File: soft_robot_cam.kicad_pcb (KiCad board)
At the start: 2 copper layers, 47.5 x 41 mm, 63 parts, among them J1 Conn_01x24_Socket, J2 Screw_Terminal_01x02, J3 Screw_Terminal_01x02, J4 Conn_01x05_Pin, J5 Screw_Terminal_01x02, Q1 S8050, Q2 S8050, SW1 reset, SW2 SW_DPST_x2, U1 DRV8872DDA, U2 DRV8872DDA, U3 ICM-20602, U4 AP2112K-1.2, U5 3.3v, U6 ESP32-WROVER-E, U7 TC2014-2.8VxCTTR

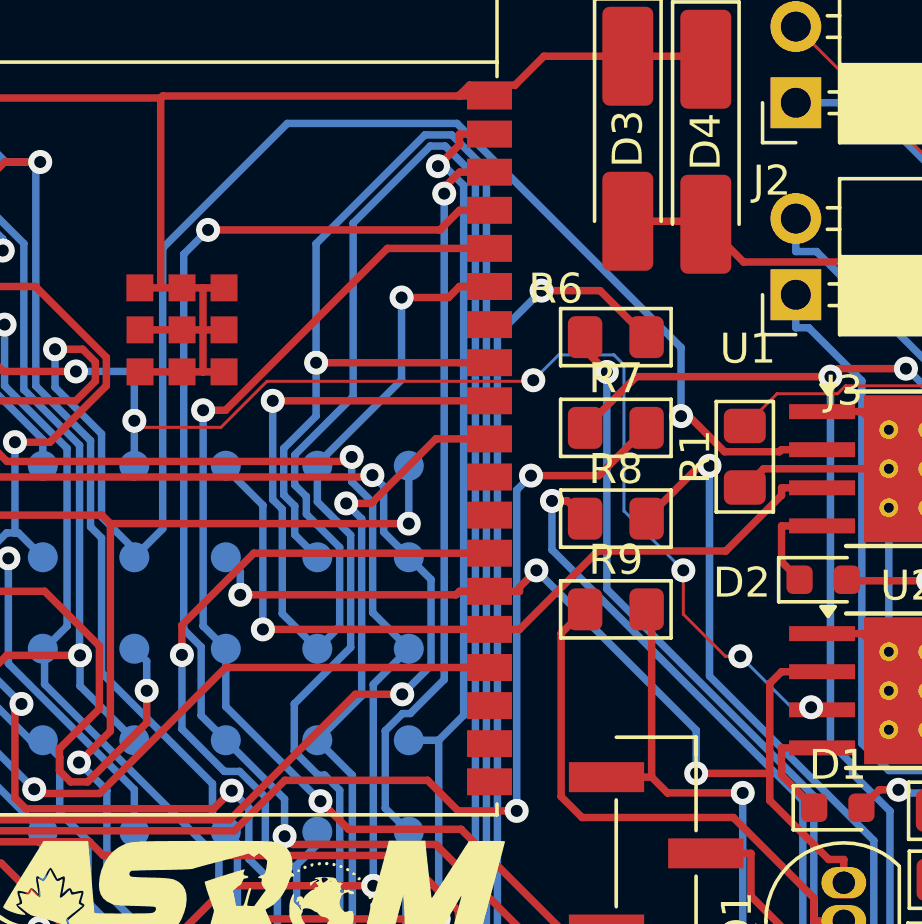
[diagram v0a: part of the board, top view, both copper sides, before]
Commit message: Major overhaul to layout, changed ESP to support more GPIOs, changed IMU to be standardized, changed LDOs to support the correct amperage, added buck converter for shifting LiPo voltage to 3.3V.
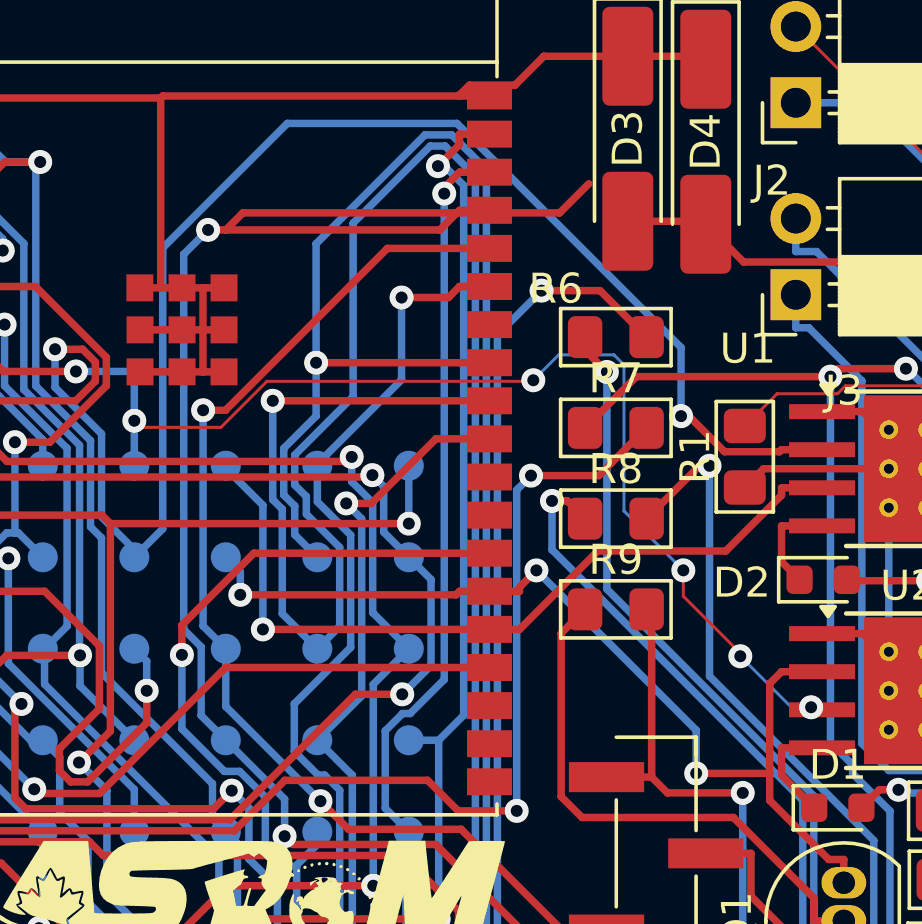
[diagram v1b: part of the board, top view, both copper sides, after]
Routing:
- net TXD_esp: track 48.0 -> 60.7 mm

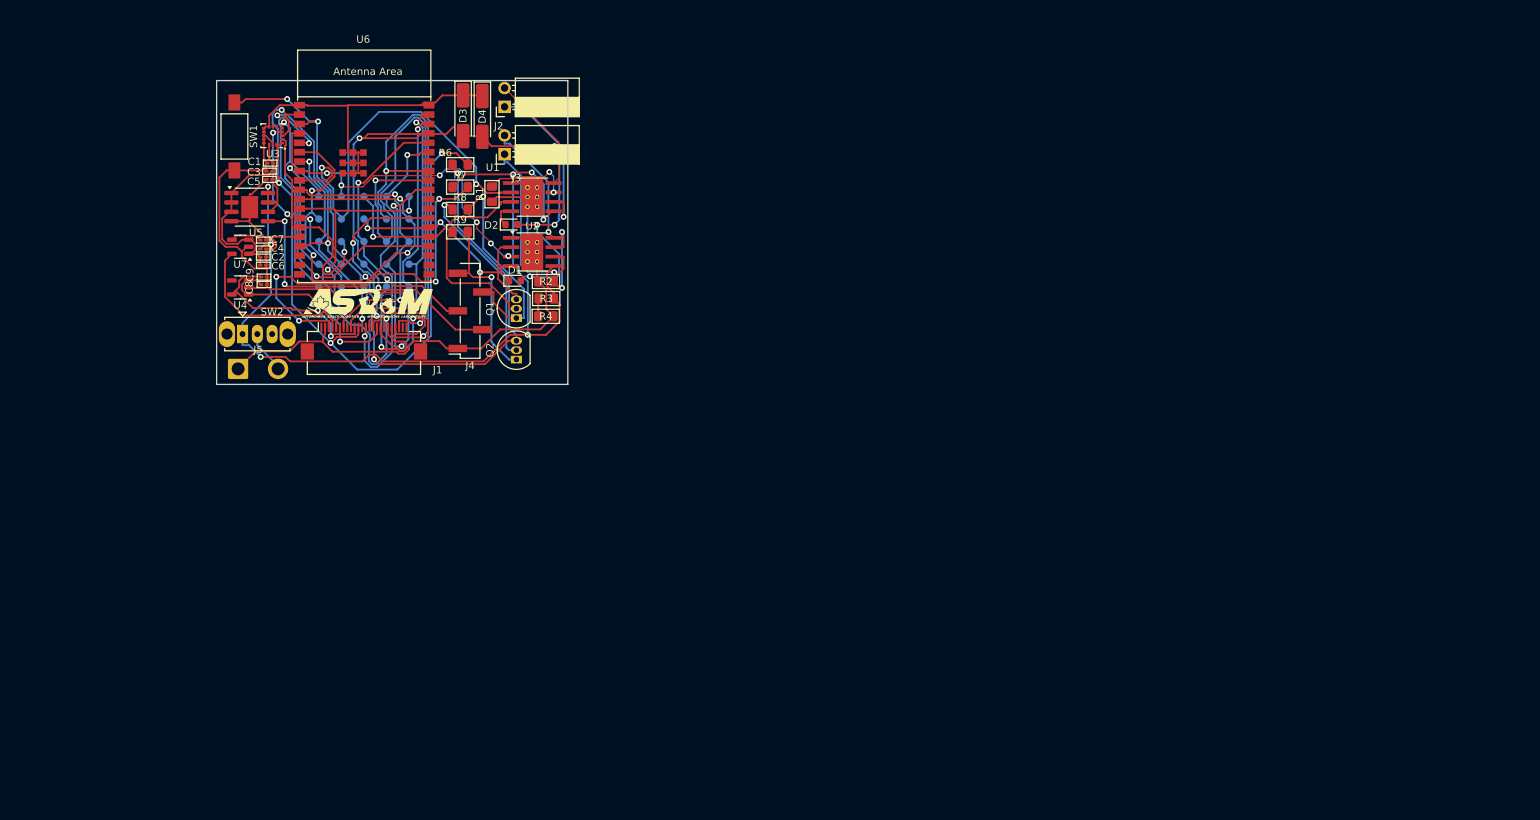
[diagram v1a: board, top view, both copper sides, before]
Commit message: Completed the schematic, began layout
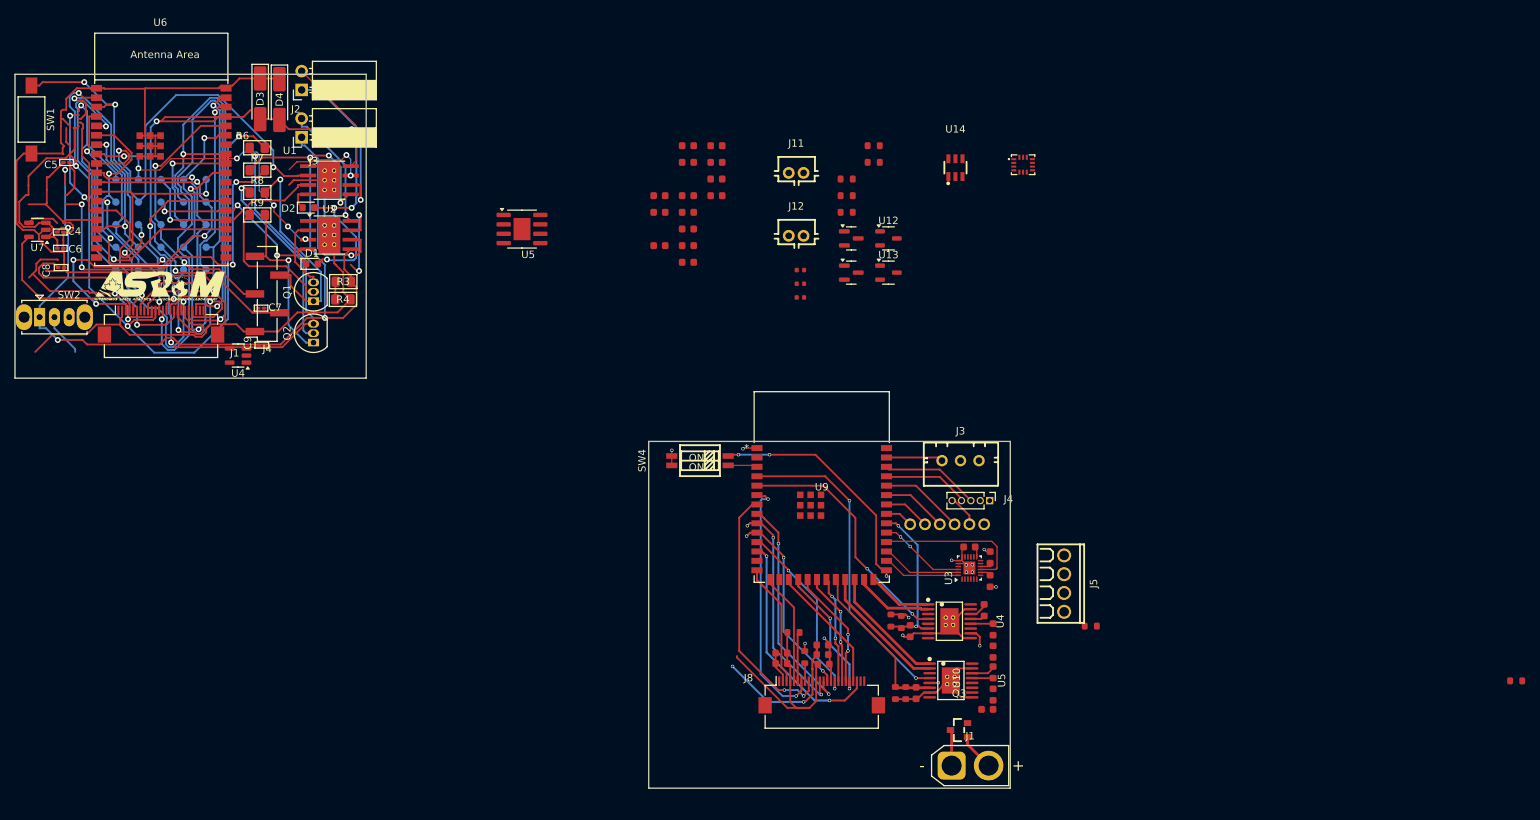
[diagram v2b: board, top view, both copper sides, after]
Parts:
- added C10: 22uF, PCM_JLCPCB:C_0603, F.Cu at (163.8, 75.2)
- added C11: 100nF, PCM_JLCPCB:C_0603, F.Cu at (163.8, 77.5)
- added C12: 100nF, PCM_JLCPCB:C_0603, F.Cu at (205.0, 143.6)
- added C13: 1uF, PCM_JLCPCB:C_0603, F.Cu at (163.8, 82.0)
- added C14: 10nF, PCM_JLCPCB:C_0603, F.Cu at (163.8, 84.2)
- added C15: 100nF, PCM_JLCPCB:C_0603, F.Cu at (163.8, 86.5)
- added C16: 2.2uF, PCM_JLCPCB:C_0603, F.Cu at (163.8, 88.8)
- added C17: 1uF, PCM_JLCPCB:C_0603, F.Cu at (163.8, 91.0)
- added C18: 1uF, PCM_JLCPCB:C_0603, F.Cu at (167.6, 75.2)
- added C19: 1uF, PCM_JLCPCB:C_0603, F.Cu at (167.6, 77.5)
- added C20: 1uF, PCM_JLCPCB:C_0603, F.Cu at (167.6, 79.8)
- added C21: 100nF, PCM_JLCPCB:C_0603, F.Cu at (167.6, 82.0)
- added C22: 10nF, PCM_JLCPCB:C_0603, F.Cu at (193.8, 140.8)
- added C23: 2.2uF, PCM_JLCPCB:C_0603, F.Cu at (176.4, 145.2)
- added C24: 2.2uF, PCM_JLCPCB:C_0603, F.Cu at (176.4, 143.8)
- added C25: 2.2uF, PCM_JLCPCB:C_0603, F.Cu at (182.1, 145.3)
- added C26: 2.2uF, PCM_JLCPCB:C_0603, F.Cu at (182.0, 142.7)
- added C27: 10nF, PCM_JLCPCB:C_0603, F.Cu at (194.6, 149.2)
- added C28: 22nF, PCM_JLCPCB:C_0603, F.Cu at (205.0, 146.4)
- added C29: 100nF, PCM_JLCPCB:C_0603, F.Cu at (205.0, 149.4)
- added C30: 100nF, PCM_JLCPCB:C_0603, F.Cu at (204.2, 151.4)
- added C31: 2.2uF, PCM_JLCPCB:C_0603, F.Cu at (182.0, 144.0)
- added C4: 220pF, PCM_JLCPCB:C_0402, F.Cu at (179.0, 92.0)
- added C5: 22uF, PCM_JLCPCB:C_0603, F.Cu at (159.9, 82.0)
- added C6: 22uF, PCM_JLCPCB:C_0603, F.Cu at (159.9, 84.2)
- added C7: 22nF, PCM_JLCPCB:C_0603, F.Cu at (203.8, 138.0)
- added C8: 10uF, PCM_JLCPCB:C_0603, F.Cu at (159.9, 88.8)
- added C9: 100nF, PCM_JLCPCB:C_0603, F.Cu at (205.0, 140.6)
- added J1: Connector, Connector_AMASS:AMASS_XT30U-F_1x02_P5.0mm_Vertical, F.Cu at (199.4, 159.0)
- added J11: Screw_Terminal_01x02, PRETTY:CONN-TH_B2B-PH-K-S, F.Cu at (178.4, 78.9)
- added J12: Screw_Terminal_01x02, PRETTY:CONN-TH_B2B-PH-K-S, F.Cu at (178.4, 87.4)
- added J2: Conn_01x06, PRETTY:CONN-TH_B6B-PH-K-S, B.Cu at (198.8, 126.4)
- added J3: Conn_01x03, easyeda2kicad:CONN-TH_3P-P2.50_A2501WV2-3P, F.Cu at (200.6, 117.8)
- added J4: Conn_01x05_Pin, Connector_PinHeader_1.27mm:PinHeader_1x05_P1.27mm_Vertical, F.Cu at (204.5, 123.2)
- added J8: Conn_01x24_Socket, Connector_FFC-FPC:Hirose_FH12-24S-0.5SH_1x24-1MP_P0.50mm_Horizontal, F.Cu at (181.8, 149.4)
- added Q1: S8050, PCM_JLCPCB:Q_SOT-23, F.Cu at (185.8, 87.8)
- added Q2: S8050, PCM_JLCPCB:Q_SOT-23, F.Cu at (185.8, 92.4)
- added Q3: AO3401A, easyeda2kicad:SOT-23_L2.9-W1.3-P1.90-LS2.4-BR, F.Cu at (200.4, 154.2)
- added R10: 10kΩ, PCM_JLCPCB:R_0603, F.Cu at (188.9, 75.2)
- added R12: 10kΩ, PCM_JLCPCB:R_0603, F.Cu at (188.9, 77.5)
- added R13: 10kΩ, PCM_JLCPCB:R_0603, F.Cu at (218.2, 140.2)
- added R14: 4.7kΩ, PCM_JLCPCB:R_0603, F.Cu at (191.2, 139.4)
- added R15: 4.7kΩ, PCM_JLCPCB:R_0603, F.Cu at (192.6, 139.6)
- added R19: 4.7kΩ, PCM_JLCPCB:R_0603, F.Cu at (191.8, 149.2)
- added R20: 4.7kΩ, PCM_JLCPCB:R_0603, F.Cu at (193.2, 149.2)
- added R21: 10kΩ, PCM_JLCPCB:R_0603, F.Cu at (275.7, 147.6)
- added R5: 100kΩ, PCM_JLCPCB:R_0402, F.Cu at (179.0, 93.9)
- added R6: 22kΩ, PCM_JLCPCB:R_0402, F.Cu at (179.0, 95.8)
- added R7: 10kΩ, PCM_JLCPCB:R_0603, F.Cu at (185.2, 79.8)
- added R8: 10kΩ, PCM_JLCPCB:R_0603, F.Cu at (185.2, 82.0)
- added R9: 10kΩ, PCM_JLCPCB:R_0603, F.Cu at (185.2, 84.2)
- added SW4: SW_DIP_x02, easyeda2kicad:SW-SMD_4P_DSHP02TSGET, F.Cu at (165.4, 117.8)
- added U10: ICM-42605, easyeda2kicad:LGA-14_L3.0-W2.5-P0.50-TL, F.Cu at (209.1, 77.8)
- added U12: XC6206P282MR, Package_TO_SOT_SMD:SOT-23-3, F.Cu at (190.9, 87.8)
- added U13: XC6206P122MR, Package_TO_SOT_SMD:SOT-23-3, F.Cu at (190.9, 92.4)
- added U14: SY8113IADC, easyeda2kicad:TSOT-23-6_L2.9-W1.6-P0.95-LS2.8-BL, F.Cu at (199.9, 78.2)
- added U4: DRV8874PWPR, easyeda2kicad:HTSSOP-16_L5.0-W4.4-P0.65-LS6.4-BL-EP, F.Cu at (199.1, 139.5)
- added U5: DRV8874PWPR, easyeda2kicad:HTSSOP-16_L5.0-W4.4-P0.65-LS6.4-BL-EP, F.Cu at (199.3, 147.5)
- added U9: ESP32-S3-WROOM-1-N16R8, esp32:ESP32-S3-WROOM-1_EXP, F.Cu at (181.8, 121.4)
- C1, C2: value 0.1uf -> 10nF; footprint PCM_Capacitor_SMD_AKL:C_0201_0603Metric_Pad0.64x0.40mm_HandSolder -> PCM_JLCPCB:C_0603
- C3: value 2.2uf -> 100nF; footprint PCM_Capacitor_SMD_AKL:C_0201_0603Metric_Pad0.64x0.40mm_HandSolder -> PCM_JLCPCB:C_0603
- J5: value Screw_Terminal_01x02 -> Screw_Terminal_01x04; footprint Connector_Wire:SolderWire-1sqmm_1x02_P5.4mm_D1.4mm_OD2.7mm -> PRETTY:CONN-TH_4P-P2.54_MX128-2.54-GN01-04P-CU-Y-A
- R1, R2: value 0.16 -> 10kΩ; footprint PCM_Resistor_SMD_AKL:R_0805_2012Metric_Pad1.15x1.40mm_HandSolder -> PCM_JLCPCB:R_0603
- U3: value ICM-20602 -> MPU6500; footprint Package_LGA:LGA-16_3x3mm_P0.5mm_LayoutBorder3x5y -> Package_DFN_QFN:QFN-24-1EP_3x3mm_P0.4mm_EP1.75x1.6mm
- moved J5 115.3 mm to (214.6, 134.4), turned to -90 degrees
- moved C1 112.5 mm to (204.6, 134.1), turned to 90 degrees
- moved U3 110.7 mm to (201.8, 132.3), turned to 90 degrees
- moved C3 107.3 mm to (201.8, 129.5), turned to 0 degrees
- moved C2 106.2 mm to (204.6, 130.9), turned to -90 degrees
- moved R1 71.9 mm to (178.0, 141.0), turned to 0 degrees
- moved R2 61.6 mm to (179.6, 144.3), turned to 90 degrees
- moved U5 36.9 mm to (141.4, 86.5)
- moved G*** 28.2 mm to (92.2, 94.0)
- moved C4 27.5 mm to (79.0, 86.9)
- moved C5 27.5 mm to (79.8, 77.5)
- moved C6 27.5 mm to (79.0, 89.1)
- moved C8 27.5 mm to (79.1, 91.7)
- moved D1 27.5 mm to (113.0, 91.2)
- moved D3 27.5 mm to (106.0, 68.9)
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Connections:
- C1 pad 1: CAM_AGND -> GND
- C1 pad 2: Net-(U3-REGOUT) -> +3.3V
- C2 pad 1: 3.3v -> GND
- C2 pad 2: CAM_AGND -> Net-(U3-REGOUT)
- C3 pad 1: 3.3v -> GND
- C3 pad 2: CAM_AGND -> +3.3V
- J5 pad 1: CAM_AGND -> /OUT1_B
- J5 pad 2: VD -> /OUT2_B
- R1 pad 1: CAM_AGND -> +2V8
- R1 pad 2: Net-(U1-ISEN) -> /RESET
- R2 pad 1: CAM_AGND -> /PWDN
- R2 pad 2: Net-(U2-ISEN) -> GND
- U3 pad 1: 3.3v -> unconnected-(U3-NC-Pad1)
- U3 pad 10: CAM_AGND -> Net-(U3-REGOUT)
- U3 pad 11: CAM_AGND -> unconnected-(U3-FSYNC-Pad11)
- U3 pad 12: CAM_AGND -> unconnected-(U3-INT-Pad12)
- U3 pad 13: CAM_AGND -> +3.3V
- U3 pad 14: Net-(U3-REGOUT) -> unconnected-(U3-NC-Pad14)
- U3 pad 15: CAM_AGND -> unconnected-(U3-NC-Pad15)
- U3 pad 16: 3.3v -> unconnected-(U3-NC-Pad16)
- U3 pad 2: IMU_SCLK -> unconnected-(U3-NC-Pad2)
- U3 pad 3: IMU_MOSI -> unconnected-(U3-NC-Pad3)
- U3 pad 4: IMU_MISO -> unconnected-(U3-NC-Pad4)
- U3 pad 5: IMU_CS -> unconnected-(U3-NC-Pad5)
- U3 pad 6: IMU_INT -> unconnected-(U3-NC-Pad6)
- U3 pad 8: CAM_AGND -> +3.3V
- U3 pad 9: CAM_AGND -> /MISO1
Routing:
- net GND: track 0.00 -> 63.6 mm, vias 0 -> 13
- net /nFAULT_B: track 0.00 -> 43.4 mm, vias 0 -> 2
- net /HREF: track 0.00 -> 34.7 mm, vias 0 -> 2
- net /VSYNC: track 0.00 -> 34.6 mm, vias 0 -> 2
- net /nFAULT_A: track 0.00 -> 33.7 mm, vias 0 -> 2
- net /BOOT: track 0.00 -> 32.6 mm, vias 0 -> 3
- net +2V8: track 0.00 -> 31.5 mm
- net /Y4: track 0.00 -> 31.1 mm, vias 0 -> 2
- net /XCLK: track 0.00 -> 30.6 mm, vias 0 -> 2
- net /Y9: track 0.00 -> 30.5 mm, vias 0 -> 3
- net /Y8: track 0.00 -> 25.9 mm, vias 0 -> 3
- net /Y7: track 0.00 -> 25.4 mm, vias 0 -> 2
- net /I_SENSE_B: track 0.00 -> 22.5 mm
- net /I_SENSE_A: track 0.00 -> 21.7 mm, vias 0 -> 2
- net /MISO1: track 0.00 -> 20.5 mm
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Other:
- board size 47.5 x 41 mm -> 134.5 x 96.5 mm

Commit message: Restitched old board, last version with old board attached, finalized layout aside from PMODE connectors.
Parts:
- removed C14: 10nF, PCM_JLCPCB:C_0603
- removed C15: 100nF, PCM_JLCPCB:C_0603
- removed C16: 2.2uF, PCM_JLCPCB:C_0603
- removed the C4 at (79.0, 86.9)
- removed the C5 at (79.8, 77.5)
- removed the C6 at (79.0, 89.1)
- removed the C8 at (79.1, 91.7)
- removed J11, J12: Screw_Terminal_01x02, PRETTY:CONN-TH_B2B-PH-K-S
- removed J5: Screw_Terminal_01x04, PRETTY:CONN-TH_4P-P2.54_MX128-2.54-GN01-04P-CU-Y-A
- removed the Q1 at (113.2, 96.3)
- removed the Q1 at (185.8, 87.8)
- removed the Q2 at (113.2, 101.9)
- removed the Q2 at (185.8, 92.4)
- removed the R6 at (105.6, 75.5)
- removed the R7 at (105.6, 78.6)
- removed the R7 at (185.2, 79.8)
- removed the R8 at (105.6, 81.6)
- removed the R8 at (185.2, 82.0)
- removed U10: ICM-42605, easyeda2kicad:LGA-14_L3.0-W2.5-P0.50-TL
- added C32: 10uF, PCM_JLCPCB:C_0603, F.Cu at (169.7, 158.6)
- added C33: 22uF, PCM_JLCPCB:C_0603, F.Cu at (160.5, 156.9)
- added C34: 10uF, PCM_JLCPCB:C_1206, F.Cu at (202.1, 144.0)
- added C35: 10uF, PCM_JLCPCB:C_1206, F.Cu at (202.6, 152.6)
- added GND: TestPoint_Pad_1.0x1.0mm, TestPoint:TestPoint_Pad_1.0x1.0mm, F.Cu at (172.8, 139.1)
- added J10: Screw_Terminal_01x02, easyeda2kicad:CONN-TH_B2B-PH-K-S, F.Cu at (167.2, 138.0)
- added J6: Screw_Terminal_01x02, easyeda2kicad:CONN-TH_B2B-PH-K-S, F.Cu at (197.4, 134.2)
- added J7: Screw_Terminal_01x02, easyeda2kicad:CONN-TH_B2B-PH-K-S, F.Cu at (197.1, 152.5)
- added J9: Screw_Terminal_01x02, easyeda2kicad:CONN-TH_B2B-PH-K-S, F.Cu at (160.4, 138.0)
- added L2: SRN6045-6R8Y, easyeda2kicad:IND-SMD_L6.0-W6.0_SRN6045, F.Cu at (165.2, 151.6)
- added Q1: S8050, PCM_JLCPCB:Q_SOT-23, F.Cu at (168.4, 128.0)
- added Q2: S8050, PCM_JLCPCB:Q_SOT-23, F.Cu at (167.1, 124.2)
- added R7: 10kΩ, PCM_JLCPCB:R_0603, F.Cu at (164.7, 126.2)
- added R8: 10kΩ, PCM_JLCPCB:R_0603, F.Cu at (166.0, 127.5)
- added REF**: MountingHole_2.2mm_M2, MountingHole:MountingHole_2.2mm_M2, F.Cu at (204.9, 117.8)
- added REF**: TestPoint_Pad_1.0x1.0mm, TestPoint:TestPoint_Pad_1.0x1.0mm, F.Cu at (193.8, 144.0)
- added REF**: MountingHole_2.2mm_M2, MountingHole:MountingHole_2.2mm_M2, F.Cu at (181.9, 159.5)
- added REF**: TestPoint_Pad_1.0x1.0mm, TestPoint:TestPoint_Pad_1.0x1.0mm, F.Cu at (178.8, 139.1)
- added REF**: TestPoint_Pad_1.0x1.0mm, TestPoint:TestPoint_Pad_1.0x1.0mm, F.Cu at (193.4, 135.6)
- added REF**: MountingHole_2.2mm_M2, MountingHole:MountingHole_2.2mm_M2, F.Cu at (161.0, 117.7)
- J2: footprint PRETTY:CONN-TH_B6B-PH-K-S -> easyeda2kicad:JST_B6B-PH-K-S; moved to F.Cu
- J3: footprint easyeda2kicad:CONN-TH_3P-P2.50_A2501WV2-3P -> easyeda2kicad:JST_B3B-PH-K-S
- U3: footprint Package_DFN_QFN:QFN-24-1EP_3x3mm_P0.4mm_EP1.75x1.6mm -> easyeda2kicad:QFN40P300X300X95-25N
- moved U14 86.5 mm to (165.7, 157.7), turned to -90 degrees
- moved R21 86.1 mm to (189.6, 145.7)
- moved C5 75.0 mm to (163.1, 156.9), turned to -90 degrees
- moved C21 73.6 mm to (165.7, 155.6)
- moved C6 72.7 mm to (161.8, 156.9), turned to -90 degrees
- moved C18 71.0 mm to (160.3, 145.9), turned to 90 degrees
- moved C8 70.4 mm to (168.4, 158.6), turned to 90 degrees
- moved C4 70.1 mm to (163.9, 160.5)
- moved R5 69.2 mm to (163.9, 161.4)
- moved R6 65.6 mm to (163.9, 159.6), turned to 180 degrees
- moved C19 65.4 mm to (165.8, 142.9), turned to -90 degrees
- moved U12 64.6 mm to (163.0, 146.1), turned to 180 degrees
- moved R10 64.5 mm to (169.7, 136.8), turned to -90 degrees
- moved C20 63.7 mm to (160.3, 143.0), turned to -90 degrees
- moved U13 57.4 mm to (163.0, 142.6), turned to 180 degrees
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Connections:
- J1 pad 1: Net-(J1-Pin_1) -> GND
- J1 pad 2: GND -> Net-(J1-Pin_2)
- J2 pad 5: GND -> +3.3V
- J2 pad 6: +3.3V -> GND
- Q3 pad 3: Net-(J1-Pin_1) -> Net-(J1-Pin_2)
- SW4 pad 1: /EN -> /BOOT
- SW4 pad 2: /BOOT -> /EN
- U9 pad 14: /I2C_SDA -> /LDR2
- U9 pad 15: /I2C_SCL -> /I2C_SDA
- U9 pad 16: /LDR2 -> /I2C_SCL
- U9 pad 22: /I_SENSE_B -> /I_SENSE_A
- U9 pad 32: /I_SENSE_A -> /I_SENSE_B
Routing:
- net +3.3V: track 4.07 -> 177.6 mm, vias 1 -> 14
- net /RXD0: track 11.5 -> 31.7 mm, vias 0 -> 1
- net /TXD0: track 13.3 -> 32.8 mm, vias 0 -> 2
- net /EN: track 3.97 -> 19.9 mm
- net /LDR1: track 0.00 -> 15.0 mm
- net /RTS: track 0.00 -> 10.6 mm
- net /OUT1_A: track 0.00 -> 9.55 mm, vias 0 -> 1
- net /BOOT: track 32.6 -> 40.6 mm
- net /I_SENSE_B: track 22.5 -> 30.5 mm, vias 0 -> 2
- net /OUT2_A: track 2.62 -> 10.5 mm
- net /LDR2: track 0.00 -> 7.72 mm
- net +1V2: track 20.2 -> 27.3 mm
- net /DTR: track 0.00 -> 7.11 mm
- net /XSHUT: track 3.78 -> 9.77 mm
- net /I_SENSE_A: track 21.7 -> 16.5 mm
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- added copper zone on F.Cu, net +3.3V
- added copper zone on F.Cu, net +7.6V
- added copper zone on In2.Cu, net +7.6V
- added copper zone on B.Cu, net GND
- added copper zone on F.Cu, net GND
- added copper zone on In1.Cu, net GND
- added copper zone on In2.Cu, net GND
- added copper zone on F.Cu, net Net-(J1-Pin_2)
- added copper zone on F.Cu, net Net-(U14-LX)
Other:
- board size 134.5 x 96.5 mm -> 134.7 x 96.5 mm
- copper layers 2 -> 4
- board text added: "+3.3V"
- board text added: "1V2"
- board text added: "2V8"
- board text added: "BOOT"
- board text added: "BUCK"
- board text added: "CAM"
- board text added: "DTR"
- board text added: "EN"
- board text added: "GND"
- board text added: "GND +3.3V SCL SDA TOF_INT XSHUT"
- board text added: "LDR1"
- board text added: "LDR2"
- board text added: "PWM"
- board text added: "RESET"
- board text added: "RTS"
- board text added: "RX"
- board text added: "TX"
